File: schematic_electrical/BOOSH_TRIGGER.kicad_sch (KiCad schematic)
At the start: 15 parts, among them Q1 FQP27P06, Q2 FQP27P06, U4 ULN2803A

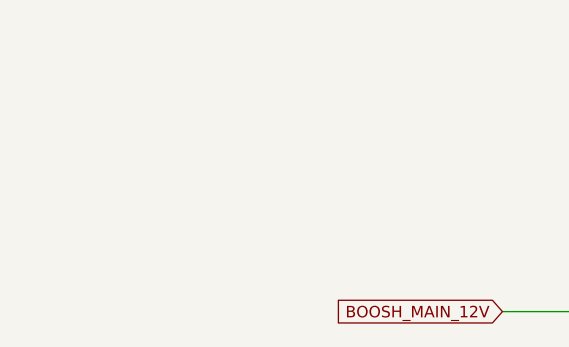
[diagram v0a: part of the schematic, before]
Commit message: Pylon schmatic: clarify filenames and add orange text to avoid confusing other similar schematic pages.
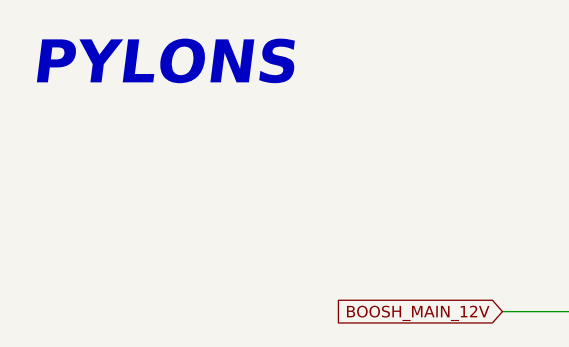
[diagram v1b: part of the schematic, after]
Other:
- note added: "PYLONS"
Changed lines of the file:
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@@
+		)
+	)
+	(text "PYLONS"
+		(exclude_from_sim no)
+		(at 29.718 20.828 0)
+		(effects
+			(font
+				(size 4.7752 4.7752)
+				(thickness 0.955)
+				(bold yes)
+				(italic yes)
+				(color 255 153 0 1)
+			)
 		)
 	)
@@
 		)
 		(instances
-			(project "high_striker_boosh"
+			(project "pylons_boosh_remote_reciver"
 				(path "/f3653ac0-a28a-4ee8-bcf5-236139001455/abf3116a-5807-45c2-900d-76b411163732"
 					(reference "#PWR042")
@@
 		)
 		(instances
-			(project "high_striker_boosh"
+			(project "pylons_boosh_remote_reciver"
 				(path "/f3653ac0-a28a-4ee8-bcf5-236139001455/abf3116a-5807-45c2-900d-76b411163732"
 					(reference "#PWR058")
@@
 		)
 		(instances
-			(project "high_striker_boosh"
+			(project "pylons_boosh_remote_reciver"
 				(path "/f3653ac0-a28a-4ee8-bcf5-236139001455/abf3116a-5807-45c2-900d-76b411163732"
 					(reference "C1")
@@
 		)
 		(instances
-			(project "high_striker_boosh"
+			(project "pylons_boosh_remote_reciver"
 				(path "/f3653ac0-a28a-4ee8-bcf5-236139001455/abf3116a-5807-45c2-900d-76b411163732"
 					(reference "D1")
@@
 		)
 		(instances
-			(project "high_striker_boosh"
+			(project "pylons_boosh_remote_reciver"
 				(path "/f3653ac0-a28a-4ee8-bcf5-236139001455/abf3116a-5807-45c2-900d-76b411163732"
 					(reference "R2")
@@
 		)
 		(instances
-			(project "high_striker_boosh"
+			(project "pylons_boosh_remote_reciver"
 				(path "/f3653ac0-a28a-4ee8-bcf5-236139001455/abf3116a-5807-45c2-900d-76b411163732"
 					(reference "Q1")
@@
 		)
 		(instances
-			(project "high_striker_boosh"
+			(project "pylons_boosh_remote_reciver"
 				(path "/f3653ac0-a28a-4ee8-bcf5-236139001455/abf3116a-5807-45c2-900d-76b411163732"
 					(reference "R9")
@@
 		)
 		(instances
-			(project "high_striker_boosh"
+			(project "pylons_boosh_remote_reciver"
 				(path "/f3653ac0-a28a-4ee8-bcf5-236139001455/abf3116a-5807-45c2-900d-76b411163732"
 					(reference "Q2")
@@
 		)
 		(instances
-			(project "high_striker_boosh"
+			(project "pylons_boosh_remote_reciver"
 				(path "/f3653ac0-a28a-4ee8-bcf5-236139001455/abf3116a-5807-45c2-900d-76b411163732"
 					(reference "R1")
@@
 		)
 		(instances
-			(project "high_striker_boosh"
+			(project "pylons_boosh_remote_reciver"
 				(path "/f3653ac0-a28a-4ee8-bcf5-236139001455/abf3116a-5807-45c2-900d-76b411163732"
 					(reference "D2")
@@
 		)
 		(instances
-			(project "high_striker_boosh"
+			(project "pylons_boosh_remote_reciver"
 				(path "/f3653ac0-a28a-4ee8-bcf5-236139001455/abf3116a-5807-45c2-900d-76b411163732"
 					(reference "#PWR041")
@@
 		)
 		(instances
-			(project "high_striker_boosh"
+			(project "pylons_boosh_remote_reciver"
 				(path "/f3653ac0-a28a-4ee8-bcf5-236139001455/abf3116a-5807-45c2-900d-76b411163732"
 					(reference "#PWR034")
@@
 		)
 		(instances
-			(project "high_striker_boosh"
+			(project "pylons_boosh_remote_reciver"
 				(path "/f3653ac0-a28a-4ee8-bcf5-236139001455/abf3116a-5807-45c2-900d-76b411163732"
 					(reference "R10")
@@
 		)
 		(instances
-			(project "high_striker_boosh"
+			(project "pylons_boosh_remote_reciver"
 				(path "/f3653ac0-a28a-4ee8-bcf5-236139001455/abf3116a-5807-45c2-900d-76b411163732"
 					(reference "#PWR052")
@@
 		)
 		(instances
-			(project "high_striker_boosh"
+			(project "pylons_boosh_remote_reciver"
 				(path "/f3653ac0-a28a-4ee8-bcf5-236139001455/abf3116a-5807-45c2-900d-76b411163732"
 					(reference "R6")
@@
 		)
 		(instances
-			(project "high_striker_boosh"
+			(project "pylons_boosh_remote_reciver"
 				(path "/f3653ac0-a28a-4ee8-bcf5-236139001455/abf3116a-5807-45c2-900d-76b411163732"
 					(reference "#PWR033")
@@
 		)
 		(instances
-			(project "high_striker_boosh"
+			(project "pylons_boosh_remote_reciver"
 				(path "/f3653ac0-a28a-4ee8-bcf5-236139001455/abf3116a-5807-45c2-900d-76b411163732"
 					(reference "#PWR040")
@@
 		)
 		(instances
-			(project "high_striker_boosh"
+			(project "pylons_boosh_remote_reciver"
 				(path "/f3653ac0-a28a-4ee8-bcf5-236139001455/abf3116a-5807-45c2-900d-76b411163732"
 					(reference "D7")
@@
 		)
 		(instances
-			(project "high_striker_boosh"
+			(project "pylons_boosh_remote_reciver"
 				(path "/f3653ac0-a28a-4ee8-bcf5-236139001455/abf3116a-5807-45c2-900d-76b411163732"
 					(reference "#PWR032")
@@
 		)
 		(instances
-			(project "high_striker_boosh"
+			(project "pylons_boosh_remote_reciver"
 				(path "/f3653ac0-a28a-4ee8-bcf5-236139001455/abf3116a-5807-45c2-900d-76b411163732"
 					(reference "#PWR035")
@@
 		)
 		(instances
-			(project "high_striker_boosh"
+			(project "pylons_boosh_remote_reciver"
 				(path "/f3653ac0-a28a-4ee8-bcf5-236139001455/abf3116a-5807-45c2-900d-76b411163732"
 					(reference "D3")
@@
 		)
 		(instances
-			(project "high_striker_boosh"
+			(project "pylons_boosh_remote_reciver"
 				(path "/f3653ac0-a28a-4ee8-bcf5-236139001455/abf3116a-5807-45c2-900d-76b411163732"
 					(reference "U4")
@@
 		)
 		(instances
-			(project "high_striker_boosh"
+			(project "pylons_boosh_remote_reciver"
 				(path "/f3653ac0-a28a-4ee8-bcf5-236139001455/abf3116a-5807-45c2-900d-76b411163732"
 					(reference "#PWR039")
@@
 		)
 		(instances
-			(project "high_striker_boosh"
+			(project "pylons_boosh_remote_reciver"
 				(path "/f3653ac0-a28a-4ee8-bcf5-236139001455/abf3116a-5807-45c2-900d-76b411163732"
 					(reference "R3")
@@
 		)
 		(instances
-			(project "high_striker_boosh"
+			(project "pylons_boosh_remote_reciver"
 				(path "/f3653ac0-a28a-4ee8-bcf5-236139001455/abf3116a-5807-45c2-900d-76b411163732"
 					(reference "R7")

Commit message: Schematic for fabrication. New symbols
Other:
- note added: "5KP16A LEADS TOO THICK. USE SCREW TERMINALS"
- note removed: "TODO: 5KP16A LEADS TOO THICK. SOLDER ONTO HEADER PINS TO MAKE PLUGGABLE OR USE SCREW TERMINALS, OR LEVER NUTS"
- note removed: "TODO: RC SNUBBER IS USELESS?"
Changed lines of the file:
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@@
-		)
-	)
-	(text "TODO:\nRC SNUBBER IS USELESS?"
-		(exclude_from_sim no)
-		(at 157.48 90.932 0)
-		(effects
-			(font
-				(size 1.27 1.27)
-			)
 		)
 	)
@@
 		)
 	)
-	(text "TODO: 5KP16A LEADS TOO THICK.\nSOLDER ONTO HEADER PINS TO MAKE PLUGGABLE\nOR USE SCREW TERMINALS, OR LEVER NUTS"
+	(text "5KP16A LEADS TOO THICK.\nUSE SCREW TERMINALS"
 		(exclude_from_sim no)
 		(at 200.914 92.71 0)

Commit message: Schematic details for as built LED series resistors, BOM/NP variations for bar PYLON
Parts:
- R7: value 1K -> 2.2K
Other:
- note added: "ONE BOARD MISTAKENLY USES 1R HERE!"
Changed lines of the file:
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@@
+		)
+	)
+	(text "ONE BOARD MISTAKENLY \nUSES 1R HERE!"
+		(exclude_from_sim no)
+		(at 215.9 54.864 0)
+		(effects
+			(font
+				(size 1.27 1.27)
+			)
 		)
 	)
@@
 			)
 		)
-		(property "Value" "1K"
+		(property "Value" "2.2K"
 			(at 200.66 53.34 90)
 			(effects
